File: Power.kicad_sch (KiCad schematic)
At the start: 30 parts, among them U2 TPS546D24SRVFR

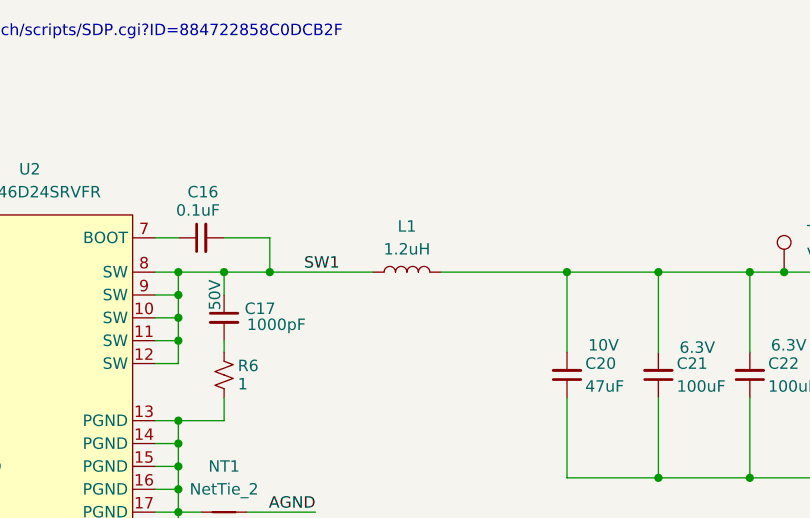
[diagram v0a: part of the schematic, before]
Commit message: add inductor footprint
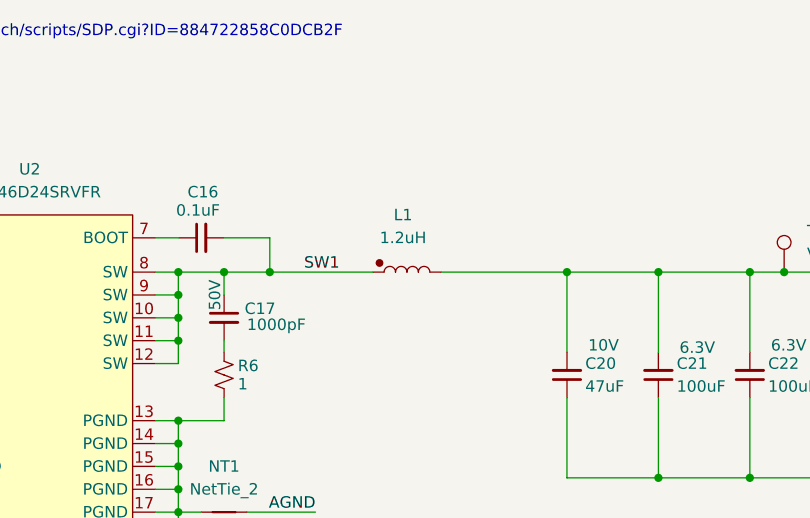
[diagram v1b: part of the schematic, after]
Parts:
- L1: symbol Device:L -> bitaxe:L-polarized
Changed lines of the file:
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@@
 	)
 	(symbol
-		(lib_id "Device:L")
-		(at 181.61 50.8 90)
+		(lib_id "bitaxe:L-polarized")
+		(at 181.61 50.8 0)
 		(unit 1)
 		(exclude_from_sim no)
@@
 		(fields_autoplaced yes)
 		(property "Reference" "L1"
-			(at 181.61 45.72 90)
+			(at 181.1764 44.45 0)
 			(effects
 				(font
@@
 		)
 		(property "Value" "1.2uH"
-			(at 181.61 48.26 90)
+			(at 181.1764 46.99 0)
 			(effects
 				(font

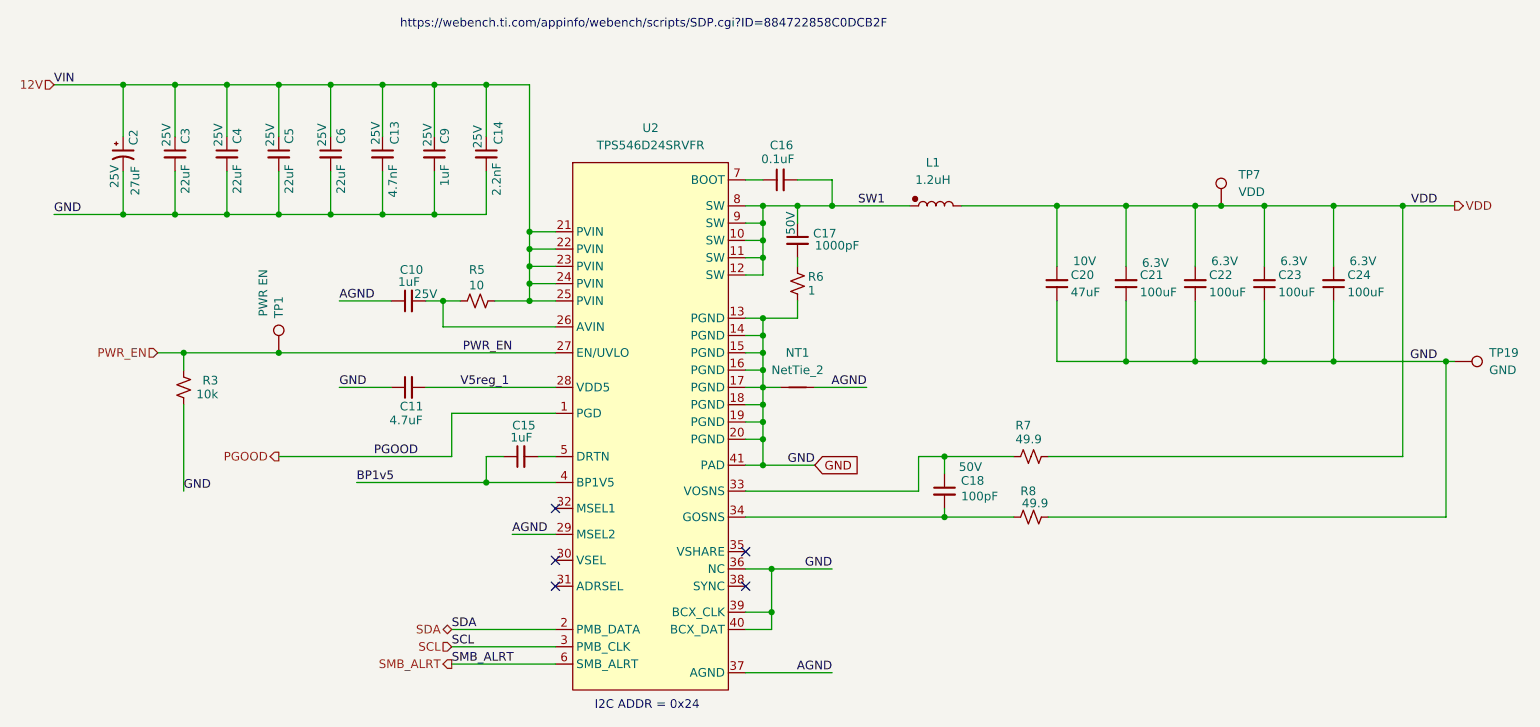
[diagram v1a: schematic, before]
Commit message: cleaned up lots of ERC errors and warnings for #4
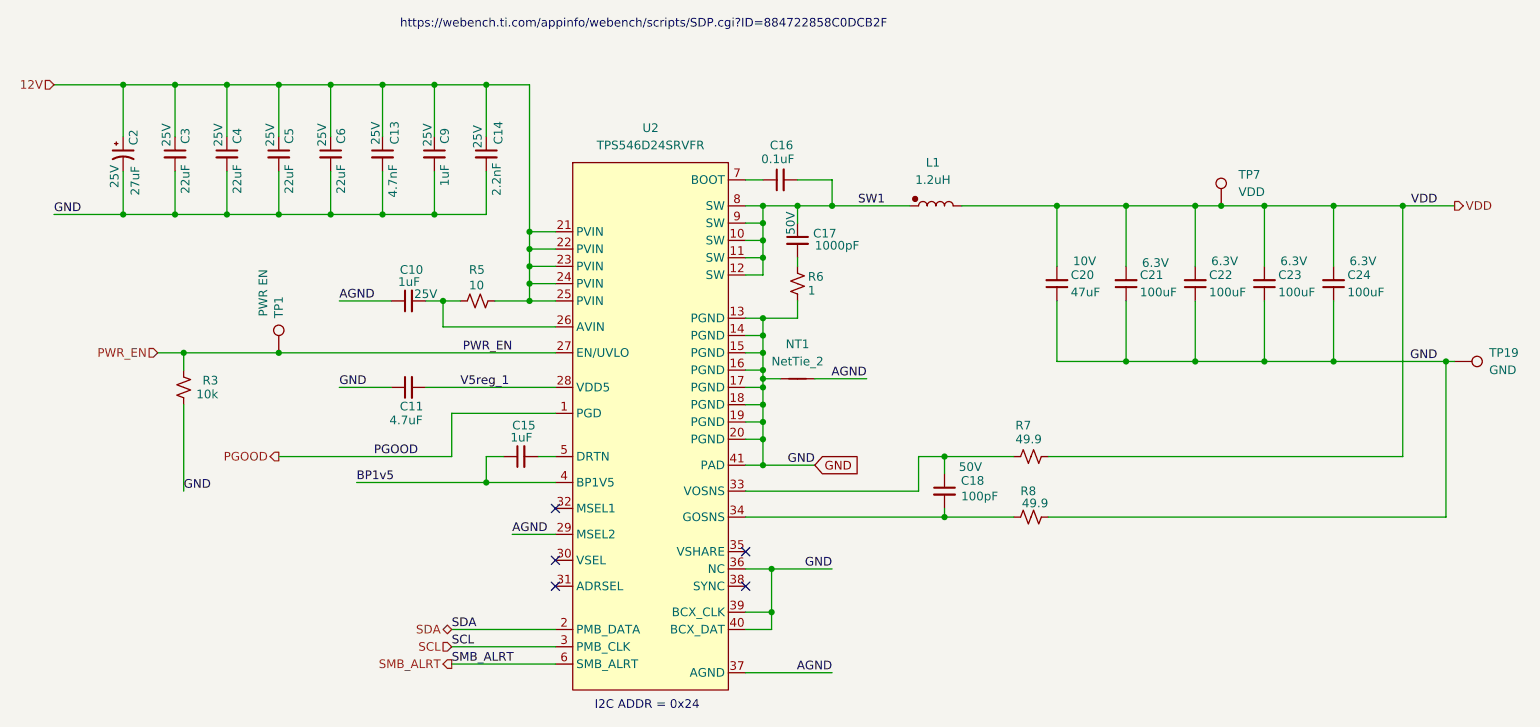
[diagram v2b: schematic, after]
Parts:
- U2: DK 296-TPS546D24SRVFRCT-ND -> 296-TPS546D24ARVFRCT-ND; PARTNO TPS546D24SRVFR -> TPS546D24ARVFR
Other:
- moved on the sheet: NT1
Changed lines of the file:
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@@
 	)
 	(junction
+		(at 156.21 76.2)
+		(diameter 0)
+		(color 0 0 0 0)
+	)
+	(junction
 		(at 157.48 104.14)
 		(diameter 0)
@@
 	(wire
 		(pts
-			(xy 156.21 77.47) (xy 158.75 77.47)
-		)
-		(stroke
-			(width 0)
-			(type default)
-		)
-	)
-	(wire
-		(pts
 			(xy 106.68 64.77) (xy 109.22 64.77)
 		)
@@
 	(wire
 		(pts
-			(xy 156.21 74.93) (xy 156.21 77.47)
+			(xy 156.21 74.93) (xy 156.21 76.2)
 		)
 		(stroke
@@
 	(wire
 		(pts
+			(xy 156.21 76.2) (xy 158.75 76.2)
+		)
+		(stroke
+			(width 0)
+			(type default)
+		)
+	)
+	(wire
+		(pts
 			(xy 240.03 50.8) (xy 250.19 50.8)
 		)
@@
 	(wire
 		(pts
-			(xy 163.83 77.47) (xy 171.45 77.47)
+			(xy 163.83 76.2) (xy 171.45 76.2)
 		)
 		(stroke
@@
 	(wire
 		(pts
+			(xy 156.21 76.2) (xy 156.21 77.47)
+		)
+		(stroke
+			(width 0)
+			(type default)
+		)
+	)
+	(wire
+		(pts
 			(xy 156.21 67.31) (xy 161.29 67.31)
 		)
@@
 		)
 	)
-	(label "VIN"
-		(at 52.07 33.02 0)
-		(effects
-			(font
-				(size 1.27 1.27)
-			)
-			(justify left bottom)
-		)
-	)
 	(label "PGOOD"
 		(at 99.06 87.63 0)
@@
 	)
 	(label "AGND"
-		(at 171.45 77.47 180)
+		(at 171.45 76.2 180)
 		(effects
 			(font
@@
 			)
 		)
-		(property "Datasheet" "https://www.yageo.com/upload/media/product/products/datasheet/rchip/PYu-RC_Group_51_RoHS_L_12.pdf"
+		(property "Datasheet" "~"
 			(at 195.58 96.52 0)
 			(effects
@@
 			)
 		)
-		(property "Datasheet" ""
+		(property "Datasheet" "~"
 			(at 62.23 43.18 0)
 			(effects
@@
 			)
 		)
-		(property "Description" "Polarized tantalum capacitor, small US symbol"
+		(property "Description" "Polarized capacitor, small US symbol"
 			(at 62.23 43.18 0)
 			(effects
@@
 			)
 		)
-		(property "Datasheet" "https://mm.digikey.com/Volume0/opasdata/d220001/medias/docus/1117/EMK105BJ105MV-F_SS.pdf"
+		(property "Datasheet" "~"
 			(at 120.65 87.63 0)
 			(effects
@@
 			)
 		)
-		(property "Datasheet" "https://datasheets.kyocera-avx.com/KGM_X7R.pdf"
+		(property "Datasheet" "~"
 			(at 182.88 92.71 0)
 			(effects
@@
 			)
 		)
-		(property "Datasheet" "https://www.yageo.com/upload/media/product/products/datasheet/rchip/PYu-RC_Group_51_RoHS_L_12.pdf"
+		(property "Datasheet" "~"
 			(at 114.3 64.77 0)
 			(effects
@@
 			)
 		)
-		(property "Datasheet" "https://mm.digikey.com/Volume0/opasdata/d220001/medias/docus/1117/EMK105BJ105MV-F_SS.pdf"
+		(property "Datasheet" "~"
 			(at 104.14 64.77 0)
 			(effects
@@
 			)
 		)
-		(property "Datasheet" "https://search.murata.co.jp/Ceramy/image/img/A01X/G101/ENG/GRM155R61H222KA01-01.pdf"
+		(property "Datasheet" "~"
 			(at 115.57 43.18 0)
 			(effects
@@
 			)
 		)
-		(property "Datasheet" "https://www.yageo.com/upload/media/product/products/datasheet/rchip/PYu-RC_Group_51_RoHS_L_12.pdf"
+		(property "Datasheet" "~"
 			(at 195.58 87.63 0)
 			(effects
@@
 			)
 		)
-		(property "Datasheet" "https://www.ti.com/lit/ds/symlink/tps546d24s.pdf"
+		(property "Datasheet" "https://www.ti.com/lit/ds/symlink/tps546d24a.pdf"
 			(at 139.7 46.99 0)
 			(effects
@@
 			)
 		)
-		(property "DK" "296-TPS546D24SRVFRCT-ND"
+		(property "DK" "296-TPS546D24ARVFRCT-ND"
 			(at 139.7 44.45 0)
 			(effects
@@
 			)
 		)
-		(property "PARTNO" "TPS546D24SRVFR"
+		(property "PARTNO" "TPS546D24ARVFR"
 			(at 139.7 41.91 0)
 			(effects
@@
 	(symbol
 		(lib_id "Device:NetTie_2")
-		(at 161.29 77.47 0)
+		(at 161.29 76.2 0)
 		(unit 1)
 		(exclude_from_sim no)
@@
 		(fields_autoplaced yes)
 		(property "Reference" "NT1"
-			(at 161.29 72.39 0)
+			(at 161.29 71.12 0)
 			(effects
 				(font
@@
 		)
 		(property "Value" "NetTie_2"
-			(at 161.29 74.93 0)
+			(at 161.29 73.66 0)
 			(effects
 				(font
@@
 		)
 		(property "Footprint" "bitaxe:NetTie-2_SMD_Pad0.2mmx1mm"
-			(at 161.29 77.47 0)
+			(at 161.29 76.2 0)
 			(effects
 				(font
@@
 		)
 		(property "Datasheet" "~"
-			(at 161.29 77.47 0)
+			(at 161.29 76.2 0)
 			(effects
 				(font
@@
 		)
 		(property "Description" "Net tie, 2 pins"
-			(at 161.29 77.47 0)
+			(at 161.29 76.2 0)
 			(effects
 				(font
@@
 		)
 		(property "Mouser" ""
-			(at 161.29 77.47 0)
+			(at 161.29 76.2 0)
 			(effects
 				(font
@@
 		)
 		(property "Manufacturer" ""
-			(at 161.29 77.47 0)
+			(at 161.29 76.2 0)
 			(effects
 				(font
@@
 			)
 		)
-		(property "Datasheet" "https://www.yageo.com/upload/media/product/products/datasheet/rchip/PYu-RC_Group_51_RoHS_L_12.pdf"
+		(property "Datasheet" "~"
 			(at 71.12 77.47 0)
 			(effects
@@
 			)
 		)
-		(property "Datasheet" "https://datasheets.kyocera-avx.com/KGM_X7R.pdf"
+		(property "Datasheet" "~"
 			(at 158.75 46.99 0)
 			(effects
@@
 			)
 		)
-		(property "Datasheet" "https://fscdn.rohm.com/en/products/databook/datasheet/passive/resistor/chip_resistor/esr-e.pdf"
+		(property "Datasheet" "~"
 			(at 161.29 62.23 0)
 			(effects
@@
 			)
 		)
-		(property "Datasheet" "https://mm.digikey.com/Volume0/opasdata/d220001/medias/docus/1117/EMK105BJ105MV-F_SS.pdf"
+		(property "Datasheet" "~"
 			(at 107.95 43.18 0)
 			(effects
@@
 			)
 		)
-		(property "Datasheet" "https://search.murata.co.jp/Ceramy/image/img/A01X/G101/ENG/GRM155R71E472KA01-01.pdf"
+		(property "Datasheet" "~"
 			(at 100.33 43.18 0)
 			(effects
@@
 			)
 		)
-		(property "Datasheet" "https://search.murata.co.jp/Ceramy/image/img/A01X/G101/ENG/GRM155R61A475MEAA-01.pdf"
+		(property "Datasheet" "~"
 			(at 104.14 77.47 0)
 			(effects
@@
 			)
 		)
-		(property "Datasheet" "https://www.yageo.com/upload/media/product/productsearch/datasheet/mlcc/UPY-GPHC_X7R_6.3V-to-250V_24.pdf"
+		(property "Datasheet" "~"
 			(at 161.29 55.88 0)
 			(effects
